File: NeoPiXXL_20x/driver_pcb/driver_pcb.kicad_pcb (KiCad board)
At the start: 2 copper layers, 20 x 10 mm, 13 parts, among them U1 WS2811

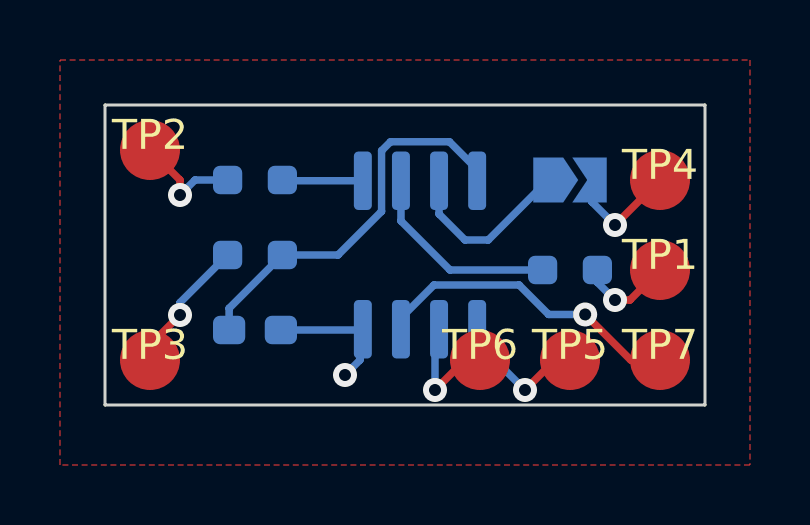
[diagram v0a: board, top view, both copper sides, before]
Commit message: fixed DOUT/DIN swap for 20x variant
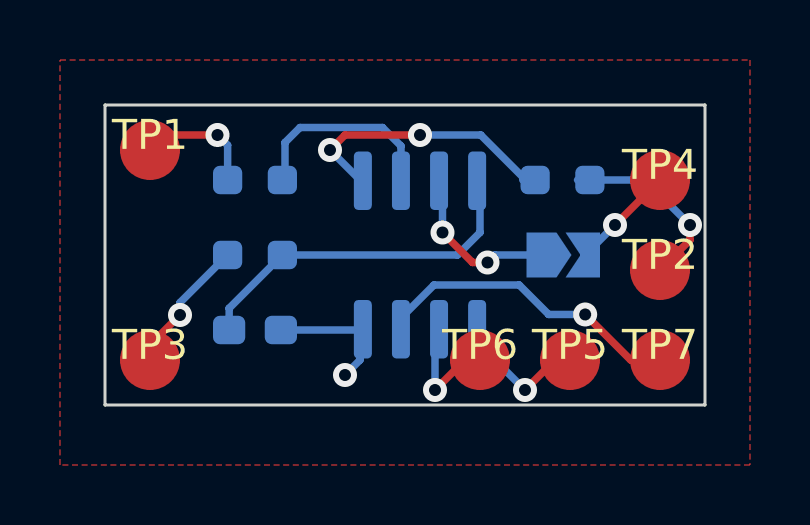
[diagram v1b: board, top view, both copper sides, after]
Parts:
- moved TP1 17.5 mm to (91.5, 71.5)
- moved TP2 17.5 mm to (108.5, 75.5)
- moved R1 10.9 mm to (95.0, 72.5), turned to 0 degrees
- moved R2 10.2 mm to (105.2, 72.5), turned to 180 degrees
- moved JP1 2.51 mm to (105.3, 75.0)
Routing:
- net Net-(R2-Pad2): track 2.69 -> 8.83 mm, vias 0 -> 2
- net Net-(R2-Pad1): track 3.71 -> 6.29 mm
- net Net-(C1-Pad1): track 13.2 -> 11.9 mm
- net Net-(R1-Pad1): track 3.16 -> 4.10 mm
- net Net-(JP1-Pad1): track 5.94 -> 5.34 mm, vias 0 -> 2

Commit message: include BOM
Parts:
- C1: value C_Small -> 100n
- R1, R2: value R_Small -> 33R
- R3: value R_Small -> 100R
- TP5: value TestPoint -> Red
- TP6: value TestPoint -> Green
- TP7: value TestPoint -> Blue
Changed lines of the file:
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@@
+      (effects (font (size 1 1) (thickness 0.15)))
+    )
+    (fp_text value "Red" (at 0 1 unlocked) (layer "F.Fab")
+      (effects (font (size 1 1) (thickness 0.15)))
+    )
+    (pad "1" smd circle (at 0 0) (size 2 2) (layers "F.Cu" "F.Paste" "F.Mask")
+      (net 5 "Net-(TP5-Pad1)") (pinfunction "1") (pintype "passive"))
+  )
+  (footprint "prints:WirePad" (layer "F.Cu")
+    (at 91.5 71.5)
+    (property "Sheetfile" "driver_pcb.kicad_sch")
+    (property "Sheetname" "")
+    (attr smd)
+    (fp_text reference "TP1" (at 0 -0.5 unlocked) (layer "F.SilkS")
       (effects (font (size 1 1) (thickness 0.15)))
     )
@@
     )
     (pad "1" smd circle (at 0 0) (size 2 2) (layers "F.Cu" "F.Paste" "F.Mask")
-      (net 5 "Net-(TP5-Pad1)") (pinfunction "1") (pintype "passive"))
-  )
-  (footprint "prints:WirePad" (layer "F.Cu")
-    (at 91.5 71.5)
-    (property "Sheetfile" "driver_pcb.kicad_sch")
-    (property "Sheetname" "")
-    (attr smd)
-    (fp_text reference "TP1" (at 0 -0.5 unlocked) (layer "F.SilkS")
+      (net 4 "Net-(R1-Pad1)") (pinfunction "1") (pintype "passive"))
+  )
+  (footprint "prints:WirePad" (layer "F.Cu")
+    (at 108.5 72.5)
+    (property "Sheetfile" "driver_pcb.kicad_sch")
+    (property "Sheetname" "")
+    (attr smd)
+    (fp_text reference "TP4" (at 0 -0.5 unlocked) (layer "F.SilkS")
       (effects (font (size 1 1) (thickness 0.15)))
     )
@@
     )
     (pad "1" smd circle (at 0 0) (size 2 2) (layers "F.Cu" "F.Paste" "F.Mask")
-      (net 4 "Net-(R1-Pad1)") (pinfunction "1") (pintype "passive"))
-  )
-  (footprint "prints:WirePad" (layer "F.Cu")
-    (at 108.5 72.5)
-    (property "Sheetfile" "driver_pcb.kicad_sch")
-    (property "Sheetname" "")
-    (attr smd)
-    (fp_text reference "TP4" (at 0 -0.5 unlocked) (layer "F.SilkS")
-      (effects (font (size 1 1) (thickness 0.15)))
-    )
-    (fp_text value "TestPoint" (at 0 1 unlocked) (layer "F.Fab")
-      (effects (font (size 1 1) (thickness 0.15)))
-    )
-    (pad "1" smd circle (at 0 0) (size 2 2) (layers "F.Cu" "F.Paste" "F.Mask")
       (net 11 "Earth") (pinfunction "1") (pintype "passive"))
   )
@@
       (effects (font (size 1 1) (thickness 0.15)))
     )
-    (fp_text value "TestPoint" (at 0 1 unlocked) (layer "F.Fab")
+    (fp_text value "Green" (at 0 1 unlocked) (layer "F.Fab")
       (effects (font (size 1 1) (thickness 0.15)))
     )
@@
       (effects (font (size 1 1) (thickness 0.15)))
     )
-    (fp_text value "TestPoint" (at 0 1 unlocked) (layer "F.Fab")
+    (fp_text value "Blue" (at 0 1 unlocked) (layer "F.Fab")
       (effects (font (size 1 1) (thickness 0.15)))
     )
@@
       (effects (font (size 1 1) (thickness 0.15)) (justify mirror))
     )
-    (fp_text value "R_Small" (at 0 -1.43) (layer "B.Fab")
+    (fp_text value "33R" (at 0 -1.43) (layer "B.Fab")
       (effects (font (size 1 1) (thickness 0.15)) (justify mirror))
     )
@@
       (effects (font (size 1 1) (thickness 0.15)) (justify mirror))
     )
-    (fp_text value "R_Small" (at 0 -1.43) (layer "B.Fab")
+    (fp_text value "100R" (at 0 -1.43) (layer "B.Fab")
       (effects (font (size 1 1) (thickness 0.15)) (justify mirror))
     )
@@
       (effects (font (size 1 1) (thickness 0.15)) (justify mirror))
     )
-    (fp_text value "C_Small" (at 0 -1.43) (layer "B.Fab")
+    (fp_text value "100n" (at 0 -1.43) (layer "B.Fab")
       (effects (font (size 1 1) (thickness 0.15)) (justify mirror))
     )
@@
       (effects (font (size 1 1) (thickness 0.15)) (justify mirror))
     )
-    (fp_text value "R_Small" (at 0 -1.43) (layer "B.Fab")
-      (effects (font (size 1 1) (thickness 0.15)) (justify mirror))
-    )
+    (fp_text value "33R" (at 0 -1.43) (layer "B.Fab")
+      (effects (font (size 1 1) (thickness 0.15)) (justify mirror))
+    )

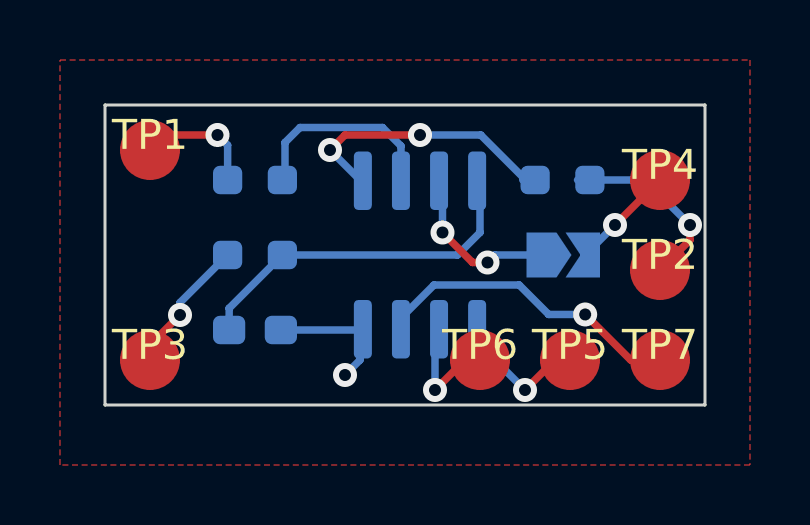
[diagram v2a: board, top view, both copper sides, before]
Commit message: Update driver for correct LED placement
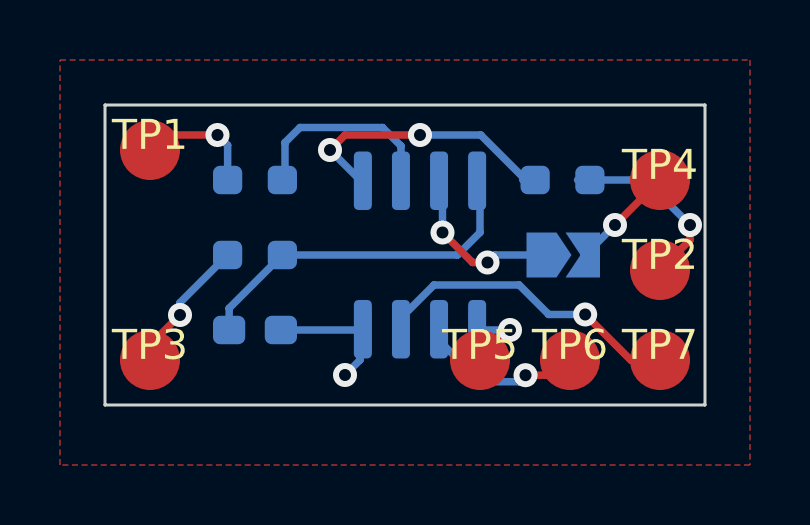
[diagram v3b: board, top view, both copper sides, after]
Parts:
- TP5: value Red -> Green
- TP6: value Green -> Red
- moved TP5 3.00 mm to (102.5, 78.5)
- moved TP6 3.00 mm to (105.5, 78.5)
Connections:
- net Net-(TP5-Pad1) renamed /G
- net Net-(TP6-Pad1) renamed /R
- net Net-(TP7-Pad1) renamed /B
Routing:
- net /G: track 4.60 -> 2.52 mm
- net /R: track 4.00 -> 5.61 mm
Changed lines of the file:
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@@
   (net 3 "Net-(R1-Pad2)")
   (net 4 "Net-(R1-Pad1)")
-  (net 5 "Net-(TP5-Pad1)")
-  (net 6 "Net-(TP6-Pad1)")
-  (net 7 "Net-(TP7-Pad1)")
+  (net 5 "/G")
+  (net 6 "/R")
+  (net 7 "/B")
   (net 8 "Net-(R2-Pad1)")
   (net 9 "Net-(R2-Pad2)")
@@
   )
   (footprint "prints:WirePad" (layer "F.Cu")
+    (at 102.5 78.5)
+    (property "Sheetfile" "driver_pcb.kicad_sch")
+    (property "Sheetname" "")
+    (attr smd)
+    (fp_text reference "TP5" (at 0 -0.5 unlocked) (layer "F.SilkS")
+      (effects (font (size 1 1) (thickness 0.15)))
+    )
+    (fp_text value "Green" (at 0 1 unlocked) (layer "F.Fab")
+      (effects (font (size 1 1) (thickness 0.15)))
+    )
+    (pad "1" smd circle (at 0 0) (size 2 2) (layers "F.Cu" "F.Paste" "F.Mask")
+      (net 5 "/G") (pinfunction "1") (pintype "passive"))
+  )
+  (footprint "prints:WirePad" (layer "F.Cu")
+    (at 91.5 71.5)
+    (property "Sheetfile" "driver_pcb.kicad_sch")
+    (property "Sheetname" "")
+    (attr smd)
+    (fp_text reference "TP1" (at 0 -0.5 unlocked) (layer "F.SilkS")
+      (effects (font (size 1 1) (thickness 0.15)))
+    )
+    (fp_text value "TestPoint" (at 0 1 unlocked) (layer "F.Fab")
+      (effects (font (size 1 1) (thickness 0.15)))
+    )
+    (pad "1" smd circle (at 0 0) (size 2 2) (layers "F.Cu" "F.Paste" "F.Mask")
+      (net 4 "Net-(R1-Pad1)") (pinfunction "1") (pintype "passive"))
+  )
+  (footprint "prints:WirePad" (layer "F.Cu")
+    (at 108.5 72.5)
+    (property "Sheetfile" "driver_pcb.kicad_sch")
+    (property "Sheetname" "")
+    (attr smd)
+    (fp_text reference "TP4" (at 0 -0.5 unlocked) (layer "F.SilkS")
+      (effects (font (size 1 1) (thickness 0.15)))
+    )
+    (fp_text value "TestPoint" (at 0 1 unlocked) (layer "F.Fab")
+      (effects (font (size 1 1) (thickness 0.15)))
+    )
+    (pad "1" smd circle (at 0 0) (size 2 2) (layers "F.Cu" "F.Paste" "F.Mask")
+      (net 11 "Earth") (pinfunction "1") (pintype "passive"))
+  )
+  (footprint "prints:WirePad" (layer "F.Cu")
     (at 105.5 78.5)
     (property "Sheetfile" "driver_pcb.kicad_sch")
     (property "Sheetname" "")
     (attr smd)
-    (fp_text reference "TP5" (at 0 -0.5 unlocked) (layer "F.SilkS")
+    (fp_text reference "TP6" (at 0 -0.5 unlocked) (layer "F.SilkS")
       (effects (font (size 1 1) (thickness 0.15)))
     )
@@
     )
     (pad "1" smd circle (at 0 0) (size 2 2) (layers "F.Cu" "F.Paste" "F.Mask")
-      (net 5 "Net-(TP5-Pad1)") (pinfunction "1") (pintype "passive"))
-  )
-  (footprint "prints:WirePad" (layer "F.Cu")
-    (at 91.5 71.5)
-    (property "Sheetfile" "driver_pcb.kicad_sch")
-    (property "Sheetname" "")
-    (attr smd)
-    (fp_text reference "TP1" (at 0 -0.5 unlocked) (layer "F.SilkS")
-      (effects (font (size 1 1) (thickness 0.15)))
-    )
-    (fp_text value "TestPoint" (at 0 1 unlocked) (layer "F.Fab")
-      (effects (font (size 1 1) (thickness 0.15)))
-    )
-    (pad "1" smd circle (at 0 0) (size 2 2) (layers "F.Cu" "F.Paste" "F.Mask")
-      (net 4 "Net-(R1-Pad1)") (pinfunction "1") (pintype "passive"))
-  )
-  (footprint "prints:WirePad" (layer "F.Cu")
-    (at 108.5 72.5)
-    (property "Sheetfile" "driver_pcb.kicad_sch")
-    (property "Sheetname" "")
-    (attr smd)
-    (fp_text reference "TP4" (at 0 -0.5 unlocked) (layer "F.SilkS")
-      (effects (font (size 1 1) (thickness 0.15)))
-    )
-    (fp_text value "TestPoint" (at 0 1 unlocked) (layer "F.Fab")
-      (effects (font (size 1 1) (thickness 0.15)))
-    )
-    (pad "1" smd circle (at 0 0) (size 2 2) (layers "F.Cu" "F.Paste" "F.Mask")
-      (net 11 "Earth") (pinfunction "1") (pintype "passive"))
-  )
-  (footprint "prints:WirePad" (layer "F.Cu")
-    (at 102.5 78.5)
-    (property "Sheetfile" "driver_pcb.kicad_sch")
-    (property "Sheetname" "")
-    (attr smd)
-    (fp_text reference "TP6" (at 0 -0.5 unlocked) (layer "F.SilkS")
-      (effects (font (size 1 1) (thickness 0.15)))
-    )
-    (fp_text value "Green" (at 0 1 unlocked) (layer "F.Fab")
-      (effects (font (size 1 1) (thickness 0.15)))
-    )
-    (pad "1" smd circle (at 0 0) (size 2 2) (layers "F.Cu" "F.Paste" "F.Mask")
-      (net 6 "Net-(TP6-Pad1)") (pinfunction "1") (pintype "passive"))
+      (net 6 "/R") (pinfunction "1") (pintype "passive"))
   )
   (footprint "prints:WirePad" (layer "F.Cu")
@@
     )
     (pad "1" smd circle (at 0 0) (size 2 2) (layers "F.Cu" "F.Paste" "F.Mask")
-      (net 7 "Net-(TP7-Pad1)") (pinfunction "1") (pintype "passive"))
+      (net 7 "/B") (pinfunction "1") (pintype "passive"))
   )
   (footprint "Resistor_SMD:R_0603_1608Metric_Pad0.98x0.95mm_HandSolder" (layer "B.Cu")
@@
     (fp_line (start 1.95 -2.45) (end -1.95 -2.45) (layer "B.Fab") (width 0.1))
     (pad "1" smd roundrect locked (at -2.475 1.905 90) (size 1.95 0.6) (layers "B.Cu" "B.Paste" "B.Mask") (roundrect_rratio 0.25)
-      (net 5 "Net-(TP5-Pad1)") (pinfunction "OUTR") (pintype "output"))
+      (net 5 "/G") (pinfunction "OUTR") (pintype "output"))
     (pad "2" smd roundrect locked (at -2.475 0.635 90) (size 1.95 0.6) (layers "B.Cu" "B.Paste" "B.Mask") (roundrect_rratio 0.25)
-      (net 6 "Net-(TP6-Pad1)") (pinfunction "OUTG") (pintype "output"))
+      (net 6 "/R") (pinfunction "OUTG") (pintype "output"))
     (pad "3" smd roundrect locked (at -2.475 -0.635 90) (size 1.95 0.6) (layers "B.Cu" "B.Paste" "B.Mask") (roundrect_rratio 0.25)
-      (net 7 "Net-(TP7-Pad1)") (pinfunction "OUTB") (pintype "output"))
+      (net 7 "/B") (pinfunction "OUTB") (pintype "output"))
     (pad "4" smd roundrect locked (at -2.475 -1.905 90) (size 1.95 0.6) (layers "B.Cu" "B.Paste" "B.Mask") (roundrect_rratio 0.25)
       (net 11 "Earth") (pinfunction "GND") (pintype "power_in"))
@@
   (segment (start 94.0875 72.5) (end 94.0875 71.3375) (width 0.25) (layer "B.Cu") (net 4))
   (segment (start 94.0875 71.3375) (end 93.75 71) (width 0.25) (layer "B.Cu") (net 4))
-  (segment (start 105 78.5) (end 104 79.5) (width 0.25) (layer "F.Cu") (net 5))
-  (segment (start 105.5 78.5) (end 105 78.5) (width 0.25) (layer "F.Cu") (net 5))
-  (via (at 104 79.5) (size 0.8) (drill 0.4) (layers "F.Cu" "B.Cu") (net 5))
-  (segment (start 102.405 77.905) (end 102.405 77.475) (width 0.25) (layer "B.Cu") (net 5))
-  (segment (start 104 79.5) (end 102.405 77.905) (width 0.25) (layer "B.Cu") (net 5))
-  (segment (start 102 78.5) (end 101 79.5) (width 0.25) (layer "F.Cu") (net 6))
-  (segment (start 102.5 78.5) (end 102 78.5) (width 0.25) (layer "F.Cu") (net 6))
-  (via (at 101 79.5) (size 0.8) (drill 0.4) (layers "F.Cu" "B.Cu") (net 6))
-  (segment (start 101 79.5) (end 101 77.61) (width 0.25) (layer "B.Cu") (net 6))
-  (segment (start 101 77.61) (end 101.135 77.475) (width 0.25) (layer "B.Cu") (net 6))
+  (segment (start 102.5 78.5) (end 103.5 77.5) (width 0.25) (layer "F.Cu") (net 5))
+  (via (at 103.5 77.5) (size 0.8) (drill 0.4) (layers "F.Cu" "B.Cu") (net 5))
+  (segment (start 102.43 77.5) (end 102.405 77.475) (width 0.25) (layer "B.Cu") (net 5))
+  (segment (start 103.5 77.5) (end 102.43 77.5) (width 0.25) (layer "B.Cu") (net 5))
+  (segment (start 104.994193 79.005807) (end 105.5 78.5) (width 0.25) (layer "F.Cu") (net 6))
+  (segment (start 104.017422 79.005807) (end 104.994193 79.005807) (width 0.25) (layer "F.Cu") (net 6))
+  (via (at 104.017422 79.005807) (size 0.8) (drill 0.4) (layers "F.Cu" "B.Cu") (net 6))
+  (segment (start 101.135 77.851072) (end 101.135 77.475) (width 0.25) (layer "B.Cu") (net 6))
+  (segment (start 102.508439 79.224511) (end 101.135 77.851072) (width 0.25) (layer "B.Cu") (net 6))
+  (segment (start 104.017422 79.005807) (end 104.017422 79.007192) (width 0.25) (layer "B.Cu") (net 6))
+  (segment (start 103.800103 79.224511) (end 102.508439 79.224511) (width 0.25) (layer "B.Cu") (net 6))
+  (segment (start 104.017422 79.007192) (end 103.800103 79.224511) (width 0.25) (layer "B.Cu") (net 6))
   (segment (start 107.523229 78.5) (end 108.5 78.5) (width 0.25) (layer "F.Cu") (net 7))
   (segment (start 106.005807 76.982578) (end 107.523229 78.5) (width 0.25) (layer "F.Cu") (net 7))
